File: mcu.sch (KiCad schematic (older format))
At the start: 27 parts, among them SW1 PTS645VL39-2, U4 CAT24C32, U5 STM32F765VIT6, X1 ECS-TXO-3225-160-TR

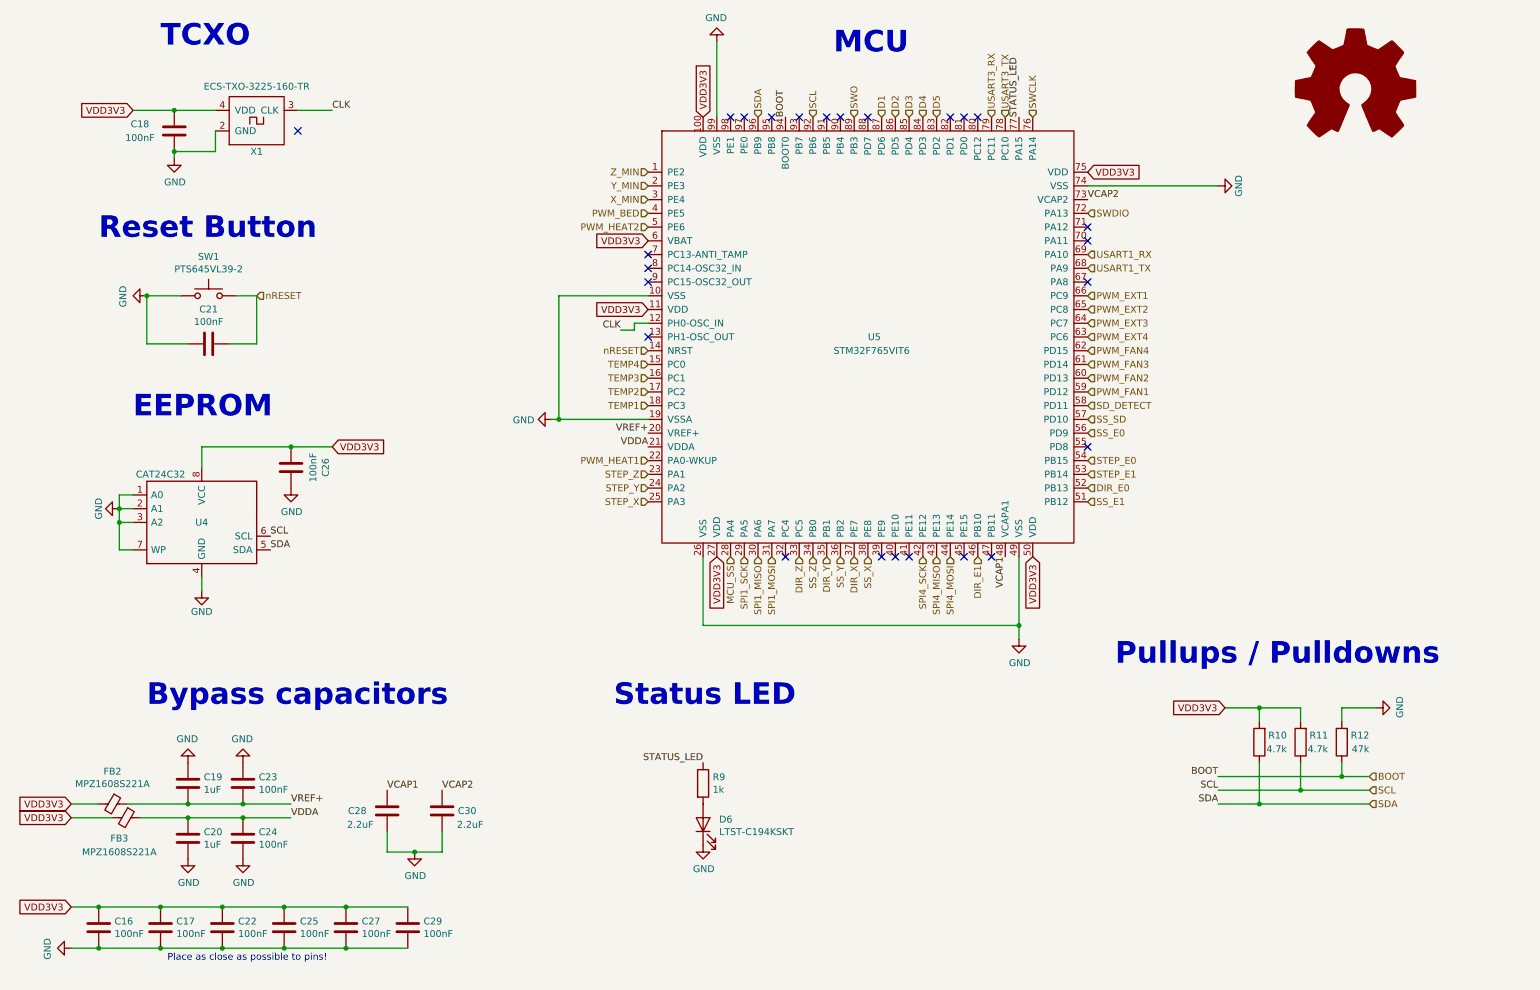
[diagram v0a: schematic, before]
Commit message: Add transistor for boot selection
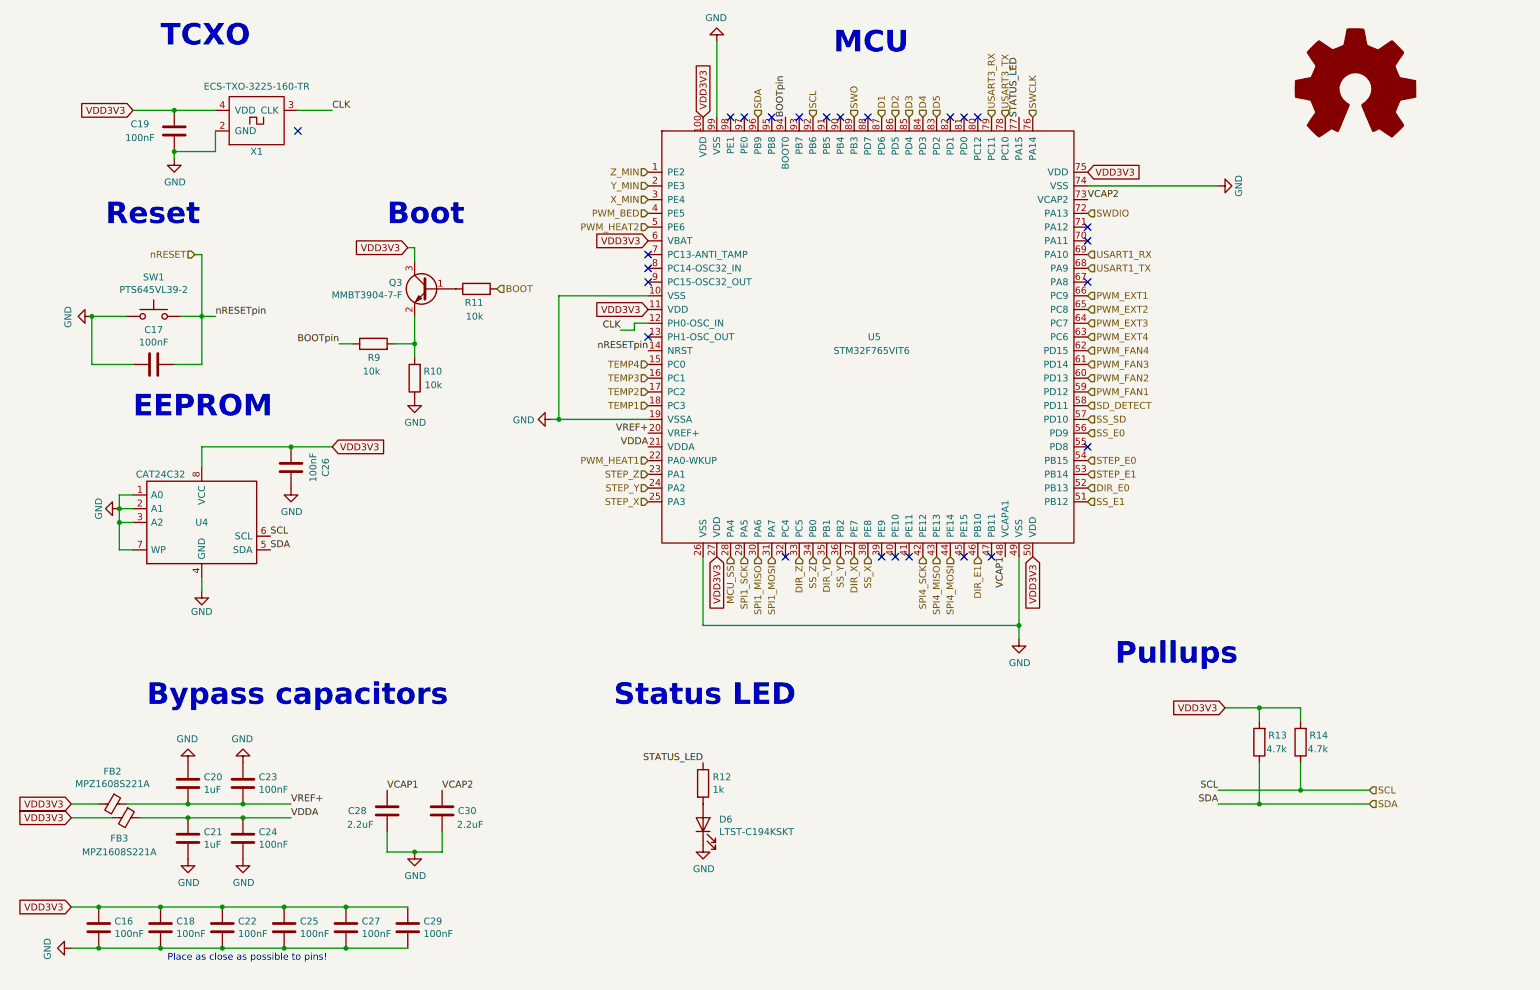
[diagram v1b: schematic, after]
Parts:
- added Q3: MMBT3904-7-F, Package_TO_SOT_SMD:SOT-23, symbol Device:Q_NPN_BEC
- added R11, R9: 10k, Resistor_SMD:R_0603_1608Metric, symbol Device:R
- R10: renamed from R12; value 47k -> 10k
- renumbered C21 to C17, C17 to C18, C18 to C19, C19 to C20, C20 to C21, R9 to R12, R10 to R13, R11 to R14
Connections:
- net BOOT: now also R11.2; no longer R10.1, U5.94 (BOOT0)
- net GND: now also R10.1; no longer R10.2
- net VDD3V3: now also Q3.3 (C)
- new net: Q3.2 (E), R10.2, R9.2
- new net: Q3.1 (B), R11.1
- new net BOOTpin: R9.1, U5.94 (BOOT0)
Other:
- note added: "Boot"
- note added: "Pullups"
- note added: "Reset"
- note removed: "Pullups / Pulldowns"
- note removed: "Reset Button"
- moved on the sheet: C17, R10, SW1
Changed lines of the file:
@@
 $EndDescr
 $Comp
-L Device:R R12
+L Device:R R10
 U 1 1 5AD0B119
-P 10200 5950
-F 0 "R12" H 10000 5900 50  0000 L CNN
-F 1 "47k" H 10000 6000 50  0000 L CNN
-F 2 "Resistor_SMD:R_0603_1608Metric" V 10130 5950 50  0001 C CNN
-F 3 "~" H 10200 5950 50  0001 C CNN
-	1    10200 5950
+P 3450 3300
+F 0 "R10" H 3250 3250 50  0000 L CNN
+F 1 "10k" H 3250 3350 50  0000 L CNN
+F 2 "Resistor_SMD:R_0603_1608Metric" V 3380 3300 50  0001 C CNN
+F 3 "~" H 3450 3300 50  0001 C CNN
+	1    3450 3300
 	-1   0    0    1
 $EndComp
@@
 VDD3V3
 $Comp
-L Device:C C20
+L Device:C C21
 U 1 1 5AD085F7
 P 1800 6650
-F 0 "C20" H 1915 6696 50  0000 L CNN
+F 0 "C21" H 1915 6696 50  0000 L CNN
 F 1 "1uF" H 1915 6605 50  0000 L CNN
 F 2 "Capacitor_SMD:C_0603_1608Metric" H 1838 6500 50  0001 C CNN
@@
 VDD3V3
 $Comp
-L Device:C C19
+L Device:C C20
 U 1 1 5AD08A76
 P 1800 6250
-F 0 "C19" H 1915 6296 50  0000 L CNN
+F 0 "C20" H 1915 6296 50  0000 L CNN
 F 1 "1uF" H 1915 6205 50  0000 L CNN
 F 2 "Capacitor_SMD:C_0603_1608Metric" H 1838 6100 50  0001 C CNN
@@
 $EndComp
 $Comp
-L Device:C C17
+L Device:C C18
 U 1 1 5AD09C8C
 P 1600 7300
-F 0 "C17" H 1715 7346 50  0000 L CNN
+F 0 "C18" H 1715 7346 50  0000 L CNN
 F 1 "100nF" H 1715 7255 50  0000 L CNN
 F 2 "Capacitor_SMD:C_0603_1608Metric" H 1638 7150 50  0001 C CNN
@@
 $EndComp
 $Comp
-L power:GND #PWR042
+L power:GND #PWR043
 U 1 1 5AF5BF00
 P 4450 3600
-F 0 "#PWR042" H 4450 3350 50  0001 C CNN
+F 0 "#PWR043" H 4450 3350 50  0001 C CNN
 F 1 "GND" V 4455 3472 50  0000 R CNN
 F 2 "" H 4450 3600 50  0001 C CNN
@@
 $EndComp
 $Comp
-L power:GND #PWR044
+L power:GND #PWR045
 U 1 1 5AF5CFF3
 P 5650 850
-F 0 "#PWR044" H 5650 600 50  0001 C CNN
+F 0 "#PWR045" H 5650 600 50  0001 C CNN
 F 1 "GND" H 5655 677 50  0000 C CNN
 F 2 "" H 5650 850 50  0001 C CNN
@@
 $EndComp
 $Comp
-L power:GND #PWR046
+L power:GND #PWR047
 U 1 1 5AF5E7FC
 P 9300 1900
-F 0 "#PWR046" H 9300 1650 50  0001 C CNN
+F 0 "#PWR047" H 9300 1650 50  0001 C CNN
 F 1 "GND" H 9300 1750 50  0000 C CNN
 F 2 "" H 9300 1900 50  0001 C CNN
@@
 $EndComp
 $Comp
-L power:GND #PWR045
+L power:GND #PWR046
 U 1 1 5AF5F2E4
 P 7850 5200
-F 0 "#PWR045" H 7850 4950 50  0001 C CNN
+F 0 "#PWR046" H 7850 4950 50  0001 C CNN
 F 1 "GND" H 7855 5027 50  0000 C CNN
 F 2 "" H 7850 5200 50  0001 C CNN
@@
 L Switch:SW_Push SW1
 U 1 1 5AF60A7F
-P 1950 2700
-F 0 "SW1" H 1950 2985 50  0000 C CNN
-F 1 "PTS645VL39-2" H 1950 2894 50  0000 C CNN
-F 2 "Button_Switch_THT:SW_Tactile_SPST_Angled_PTS645Vx39-2LFS" H 1950 2900 50  0001 C CNN
-F 3 "https://www.mouser.de/datasheet/2/60/-1131575.pdf" H 1950 2900 50  0001 C CNN
-	1    1950 2700
-	1    0    0    -1
-$EndComp
-$Comp
-L power:GND #PWR033
+P 1550 2850
+F 0 "SW1" H 1550 3135 50  0000 C CNN
+F 1 "PTS645VL39-2" H 1550 3044 50  0000 C CNN
+F 2 "Button_Switch_THT:SW_Tactile_SPST_Angled_PTS645Vx39-2LFS" H 1550 3050 50  0001 C CNN
+F 3 "https://www.mouser.de/datasheet/2/60/-1131575.pdf" H 1550 3050 50  0001 C CNN
+	1    1550 2850
+	1    0    0    -1
+$EndComp
+$Comp
+L power:GND #PWR032
 U 1 1 5AF616AA
-P 1500 2700
-F 0 "#PWR033" H 1500 2450 50  0001 C CNN
-F 1 "GND" H 1505 2527 50  0000 C CNN
-F 2 "" H 1500 2700 50  0001 C CNN
-F 3 "" H 1500 2700 50  0001 C CNN
-	1    1500 2700
+P 1100 2850
+F 0 "#PWR032" H 1100 2600 50  0001 C CNN
+F 1 "GND" H 1105 2677 50  0000 C CNN
+F 2 "" H 1100 2850 50  0001 C CNN
+F 3 "" H 1100 2850 50  0001 C CNN
+	1    1100 2850
 	0    1    1    0
 $EndComp
 Wire Wire Line
-	1500 2700 1750 2700
-$Comp
-L Device:C C21
+	1100 2850 1350 2850
+$Comp
+L Device:C C17
 U 1 1 5AF62329
-P 1950 3050
-F 0 "C21" V 2202 3050 50  0000 C CNN
-F 1 "100nF" V 2111 3050 50  0000 C CNN
-F 2 "Capacitor_SMD:C_0603_1608Metric" H 1988 2900 50  0001 C CNN
-F 3 "~" H 1950 3050 50  0001 C CNN
-	1    1950 3050
+P 1550 3200
+F 0 "C17" V 1802 3200 50  0000 C CNN
+F 1 "100nF" V 1711 3200 50  0000 C CNN
+F 2 "Capacitor_SMD:C_0603_1608Metric" H 1588 3050 50  0001 C CNN
+F 3 "~" H 1550 3200 50  0001 C CNN
+	1    1550 3200
 	0    -1   -1   0
 $EndComp
 Wire Wire Line
-	2100 3050 2300 3050
-Wire Wire Line
-	1500 2700 1500 3050
-Wire Wire Line
-	1500 3050 1800 3050
-$Comp
-L power:GND #PWR047
+	1700 3200 1900 3200
+Wire Wire Line
+	1100 2850 1100 3200
+Wire Wire Line
+	1100 3200 1400 3200
+$Comp
+L power:GND #PWR041
 U 1 1 5AF66D47
-P 10450 5700
-F 0 "#PWR047" H 10450 5450 50  0001 C CNN
-F 1 "GND" H 10455 5527 50  0000 C CNN
-F 2 "" H 10450 5700 50  0001 C CNN
-F 3 "" H 10450 5700 50  0001 C CNN
-	1    10450 5700
-	0    -1   -1   0
+P 3450 3450
+F 0 "#PWR041" H 3450 3200 50  0001 C CNN
+F 1 "GND" H 3455 3277 50  0000 C CNN
+F 2 "" H 3450 3450 50  0001 C CNN
+F 3 "" H 3450 3450 50  0001 C CNN
+	1    3450 3450
+	1    0    0    -1
 $EndComp
 $Comp
@@
 	1450 6500 1800 6500
 Connection ~ 1800 6500
-Connection ~ 1500 2700
+Connection ~ 1100 2850
 Text GLabel 8350 1800 2    50   Input ~ 0
 VDD3V3
-Text HLabel 2300 2700 2    50   Input ~ 0
+Text HLabel 1850 2400 0    50   Input ~ 0
 nRESET
 Wire Wire Line
-	2150 2700 2300 2700
-Wire Wire Line
-	2300 3050 2300 2700
+	1750 2850 1900 2850
+Wire Wire Line
+	1900 3200 1900 2850
 $Comp
 L power:GND #PWR031
@@
 	0    1    1    0
 $EndComp
-Text HLabel 10400 6200 2    50   Input ~ 0
+Text HLabel 4050 2650 2    50   Input ~ 0
 BOOT
 Text Notes 6500 950  0    157  ~ 31
@@
 $EndComp
 $Comp
-L Device:C C18
+L Device:C C19
 U 1 1 5BC55501
 P 1700 1500
-F 0 "C18" H 1450 1550 50  0000 C CNN
+F 0 "C19" H 1450 1550 50  0000 C CNN
 F 1 "100nF" H 1450 1450 50  0000 C CNN
 F 2 "Capacitor_SMD:C_0603_1608Metric" H 1738 1350 50  0001 C CNN
@@
 AR Path="/5BC1FDFA" Ref="#PWR?"  Part="1"
 AR Path="/5BC4AC32/5BC1FDFA" Ref="#PWR?"  Part="1"
-AR Path="/5BC1C8A4/5BC1FDFA" Ref="#PWR032"  Part="1"
-F 0 "#PWR032" H 1300 4000 50  0001 C CNN
+AR Path="/5BC1C8A4/5BC1FDFA" Ref="#PWR033"  Part="1"
+F 0 "#PWR033" H 1300 4000 50  0001 C CNN
 F 1 "GND" H 1300 4100 50  0000 C CNN
 F 2 "" H 1300 4250 50  0000 C CNN
@@
 Text Label 4950 2950 2    50   ~ 0
 CLK
-Text HLabel 5150 3100 0    50   Input ~ 0
-nRESET
 NoConn ~ 5150 2500
 NoConn ~ 5150 2600
 Text Notes 1600 900  0    157  ~ 31
 TCXO
-Text Notes 1150 2300 0    157  ~ 31
-Reset Button
+Text Notes 1200 2200 0    157  ~ 31
+Reset
 Text Label 2550 6400 0    50   ~ 0
 VREF+
@@
 Text Label 9300 6300 2    50   ~ 0
 SCL
-Text Label 9300 6200 2    50   ~ 0
-BOOT
-$Comp
-L Device:R R10
+Text Label 2900 3050 2    50   ~ 0
+BOOTpin
+$Comp
+L Device:R R13
 U 1 1 5BCD0D7A
 P 9600 5950
-F 0 "R10" H 9400 5900 50  0000 L CNN
+F 0 "R13" H 9400 5900 50  0000 L CNN
 F 1 "4.7k" H 9400 6000 50  0000 L CNN
 F 2 "Resistor_SMD:R_0603_1608Metric" V 9530 5950 50  0001 C CNN
@@
 VDD3V3
 $Comp
-L Device:R R11
+L Device:R R14
 U 1 1 5BCDCE1E
 P 9900 5950
-F 0 "R11" H 9700 5900 50  0000 L CNN
+F 0 "R14" H 9700 5900 50  0000 L CNN
 F 1 "4.7k" H 9700 6000 50  0000 L CNN
 F 2 "Resistor_SMD:R_0603_1608Metric" V 9830 5950 50  0001 C CNN
@@
 	9600 5700 9900 5700
 Wire Wire Line
-	10200 6100 10200 6200
-Wire Wire Line
-	10200 6200 10400 6200
-Wire Wire Line
 	9300 6400 9600 6400
 Wire Wire Line
 	9300 6300 9900 6300
-Wire Wire Line
-	10200 6200 9300 6200
-Connection ~ 10200 6200
-Wire Wire Line
-	10450 5700 10200 5700
-Wire Wire Line
-	10200 5700 10200 5800
 Wire Wire Line
 	9900 6100 9900 6300
@@
 	9600 6400 10400 6400
 Text Notes 8550 5400 0    157  ~ 31
-Pullups / Pulldowns
+Pullups
 Text Label 6150 1400 1    50   ~ 0
-BOOT
+BOOTpin
 Text Label 3250 6300 0    50   ~ 0
 VCAP1
@@
 VCAP2
 $Comp
-L power:GND #PWR041
+L power:GND #PWR042
 U 1 1 5BCFC2D0
 P 3450 6750
-F 0 "#PWR041" H 3450 6500 50  0001 C CNN
+F 0 "#PWR042" H 3450 6500 50  0001 C CNN
 F 1 "GND" H 3455 6577 50  0000 C CNN
 F 2 "" H 3450 6750 50  0001 C CNN
@@
 P 5550 6250
 AR Path="/5BC54251/5BCE7FB5" Ref="R?"  Part="1"
-AR Path="/5BC1C8A4/5BCE7FB5" Ref="R9"  Part="1"
-F 0 "R9" H 5620 6296 50  0000 L CNN
+AR Path="/5BC1C8A4/5BCE7FB5" Ref="R12"  Part="1"
+F 0 "R12" H 5620 6296 50  0000 L CNN
 F 1 "1k" H 5620 6205 50  0000 L CNN
 F 2 "Resistor_SMD:R_0603_1608Metric" V 5480 6250 50  0001 C CNN
@@
 $EndComp
 $Comp
-L power:GND #PWR043
+L power:GND #PWR044
 U 1 1 5BCEB458
 P 5550 6700
-F 0 "#PWR043" H 5550 6450 50  0001 C CNN
+F 0 "#PWR044" H 5550 6450 50  0001 C CNN
 F 1 "GND" H 5555 6527 50  0000 C CNN
 F 2 "" H 5550 6700 50  0001 C CNN
@@
 	1900 3800 2550 3800
 Connection ~ 2550 3800
+$Comp
+L Device:R R9
+U 1 1 5BD6A8E4
+P 3150 3050
+F 0 "R9" V 3050 3000 50  0000 L CNN
+F 1 "10k" V 2950 3000 50  0000 L CNN
+F 2 "Resistor_SMD:R_0603_1608Metric" V 3080 3050 50  0001 C CNN
+F 3 "~" H 3150 3050 50  0001 C CNN
+	1    3150 3050
+	0    -1   -1   0
+$EndComp
+Text Notes 3250 2200 0    157  ~ 31
+Boot
+Connection ~ 1900 2850
+Wire Wire Line
+	3300 3050 3450 3050
+Text GLabel 3400 2350 0    50   Input ~ 0
+VDD3V3
+$Comp
+L Device:Q_NPN_BEC Q3
+U 1 1 5BD9AD61
+P 3550 2650
+F 0 "Q3" H 3740 2696 50  0000 L CNN
+F 1 "MMBT3904-7-F" H 3740 2605 50  0000 L CNN
+F 2 "Package_TO_SOT_SMD:SOT-23" H 3750 2750 50  0001 C CNN
+F 3 "https://eu.mouser.com/datasheet/2/115/ds30036-41708.pdf" H 3550 2650 50  0001 C CNN
+	1    3550 2650
+	-1   0    0    -1
+$EndComp
+Wire Wire Line
+	3450 3150 3450 3050
+Wire Wire Line
+	3450 2850 3450 3050
+Connection ~ 3450 3050
+Wire Wire Line
+	3400 2350 3450 2350
+Wire Wire Line
+	3450 2350 3450 2450
+Wire Wire Line
+	2900 3050 3000 3050
+$Comp
+L Device:R R11
+U 1 1 5BDA97CE
+P 3900 2650
+F 0 "R11" V 3800 2600 50  0000 L CNN
+F 1 "10k" V 3700 2600 50  0000 L CNN
+F 2 "Resistor_SMD:R_0603_1608Metric" V 3830 2650 50  0001 C CNN
+F 3 "~" H 3900 2650 50  0001 C CNN
+	1    3900 2650
+	0    -1   -1   0
+$EndComp
+Text Label 5150 3100 2    50   ~ 0
+nRESETpin
+Text Label 2000 2850 0    50   ~ 0
+nRESETpin
+Wire Wire Line
+	1900 2850 1900 2400
+Wire Wire Line
+	1900 2400 1850 2400
+Wire Wire Line
+	2000 2850 1900 2850
 $EndSCHEMATC

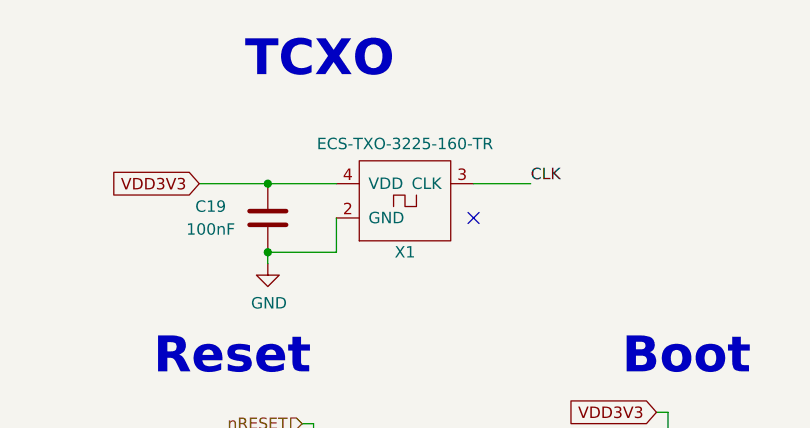
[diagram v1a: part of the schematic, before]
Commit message: Update TXCO and STM32CubeMX configuration file
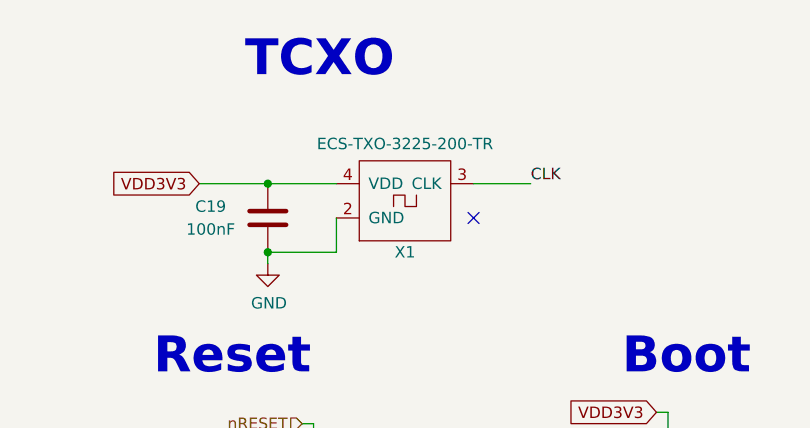
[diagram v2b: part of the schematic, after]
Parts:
- X1: value ECS-TXO-3225-160-TR -> ECS-TXO-3225-200-TR
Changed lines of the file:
@@
 P 2300 1350
 F 0 "X1" H 2300 1050 50  0000 C CNN
-F 1 "ECS-TXO-3225-160-TR" H 2300 1524 50  0000 C CNN
+F 1 "ECS-TXO-3225-200-TR" H 2300 1524 50  0000 C CNN
 F 2 "heteromycin:ECS-TXO-3225" H 2300 1350 157 0001 C CNN
 F 3 "https://www.ecsxtal.com/store/pdf/ECS-TXO-3225.pdf" H 2300 1350 157 0001 C CNN

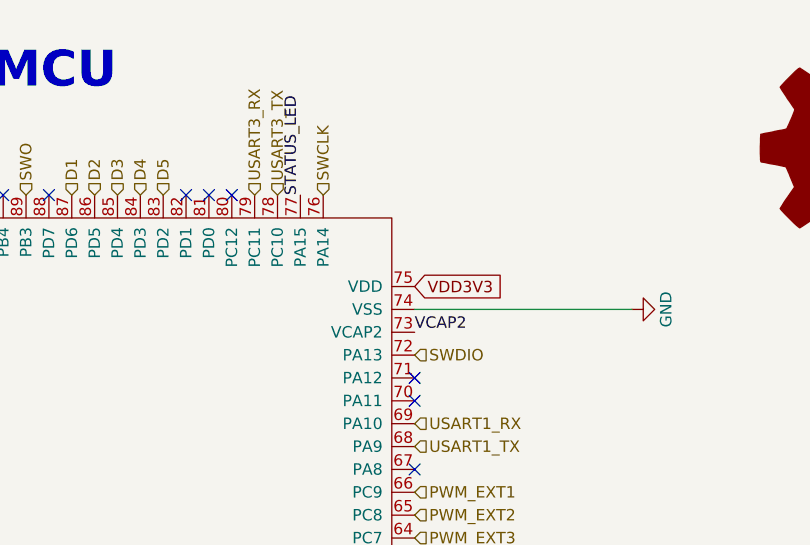
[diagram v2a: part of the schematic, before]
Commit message: Updated board to version 1.2
 * Switched small MOSFETs to SOT-23 package
 * Redesigned TMC*160 driver layout
 * Changed 01x03 to 02x03 jumper for FAN voltage selection
 * Switches STATUS_LED pin
 * Some copper pour optimizations
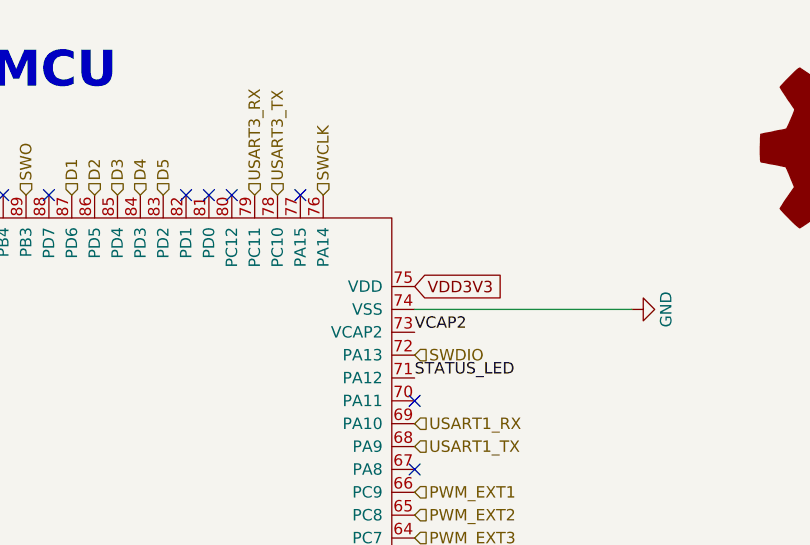
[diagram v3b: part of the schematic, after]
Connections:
- net STATUS_LED: now also U5.71 (PA12); no longer U5.77 (PA15)
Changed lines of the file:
@@
 SS_SD
 NoConn ~ 8350 2600
-NoConn ~ 8350 2200
 Text HLabel 8350 2100 2    50   Input ~ 0
 SWDIO
@@
 D5
 NoConn ~ 7350 1400
-Text Label 7850 1400 1    50   ~ 0
+Text Label 8350 2200 0    50   ~ 0
 STATUS_LED
 Text Label 5550 6100 2    50   ~ 0
@@
 Wire Wire Line
 	2000 2850 1900 2850
+NoConn ~ 7850 1400
 $EndSCHEMATC
